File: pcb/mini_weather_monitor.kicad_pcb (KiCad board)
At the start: 2 copper layers, 135 x 72 mm, 28 parts, among them J1 Conn_01x02, Q1 IRLML6402, U2 4.0inch_SPI_MSP4021, U2_BME280 module_bme280, U3_BH1750 module_bh1750

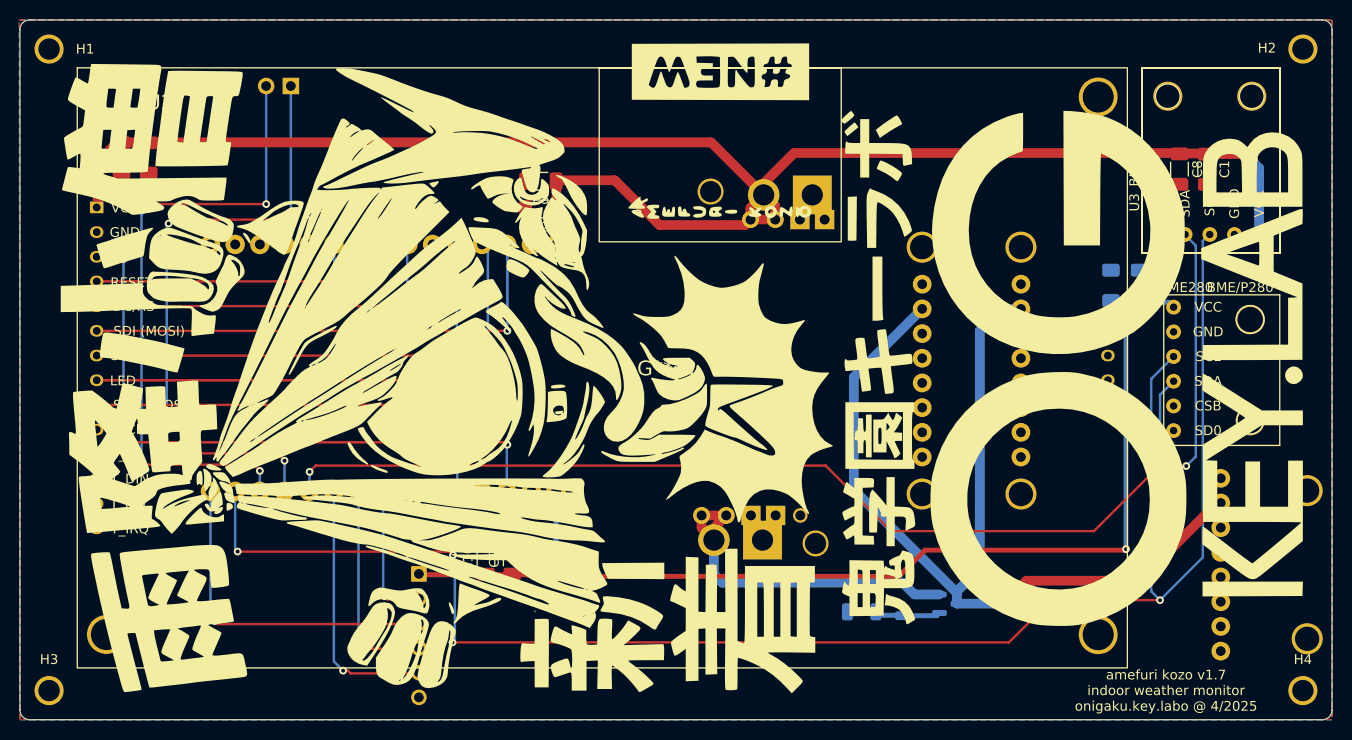
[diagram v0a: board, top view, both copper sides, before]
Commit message: adding passthrough
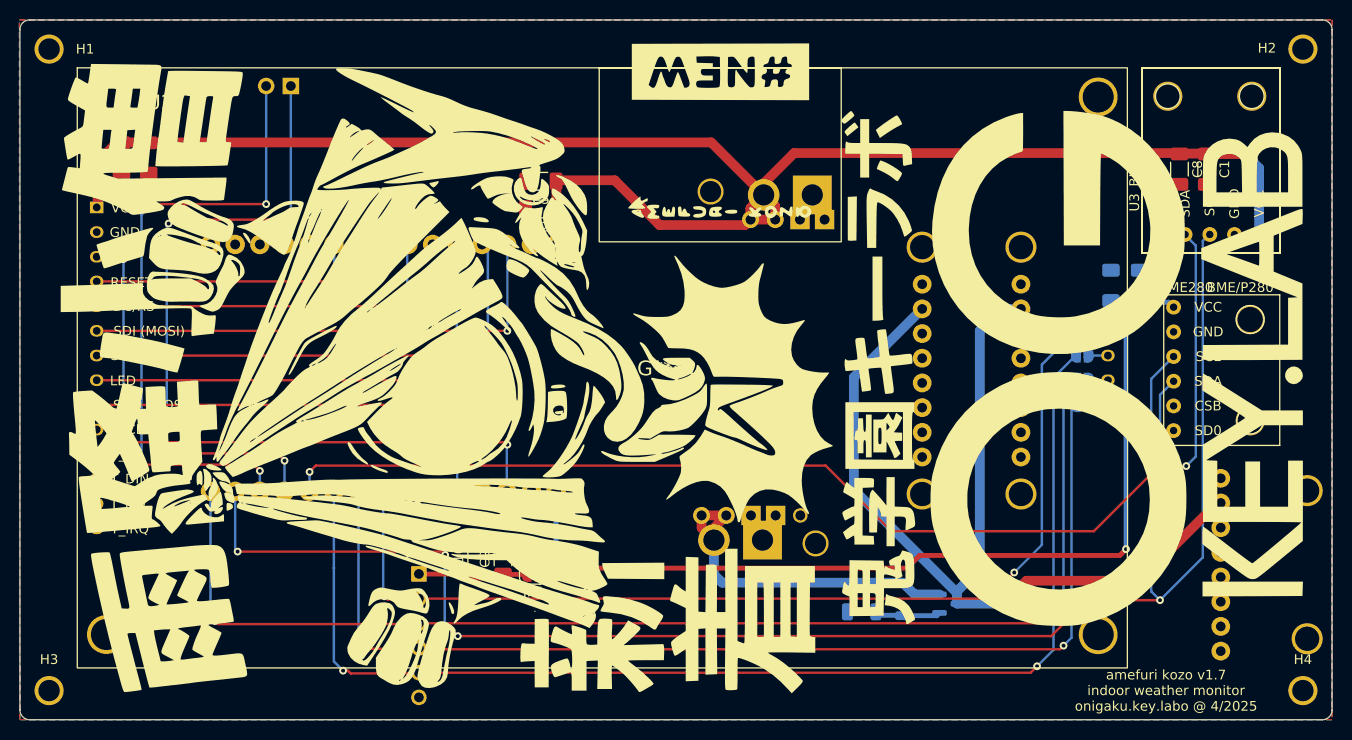
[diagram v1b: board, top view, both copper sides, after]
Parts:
- added JP5: sj_mini_3v3, Jumper:SolderJumper-2_P1.3mm_Open_RoundedPad1.0x1.5mm, F.Cu at (118.8, 121.0)
- added JP6: sj_Open_onboard_sdcard_MOSI, Jumper:SolderJumper-2_P1.3mm_Open_RoundedPad1.0x1.5mm, B.Cu at (175.3, 98.5)
- added JP7: sj_Open_onboard_sdcard_MISO, Jumper:SolderJumper-2_P1.3mm_Open_RoundedPad1.0x1.5mm, B.Cu at (175.3, 101.0)
- added JP8: sj_Open_onboard_sdcard_CS, Jumper:SolderJumper-2_P1.3mm_Open_RoundedPad1.0x1.5mm, B.Cu at (175.3, 96.0)
- added JP9: sj_onboard_sdcard_clk, Jumper:SolderJumper-2_P1.3mm_Open_RoundedPad1.0x1.5mm, B.Cu at (175.3, 103.6)
- moved C10 0.95 mm to (113.0, 119.5)
- moved C9 0.95 mm to (115.7, 119.5)
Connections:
- C10 pad 1: +3V3 -> Net-(JP5-B)
- C9 pad 1: +3V3 -> Net-(JP5-B)
- U2 pad 15: unconnected-(U2-SD_CS-Pad15) -> Net-(JP8-A)
- U2 pad 16: unconnected-(U2-SD_MOSI-Pad16) -> Net-(JP6-A)
- U2 pad 17: unconnected-(U2-SD_MISO-Pad17) -> Net-(JP7-A)
- U2 pad 18: unconnected-(U2-SD_SCK-Pad18) -> Net-(JP9-A)
- U3_minisdcard1 pad 1: +3V3 -> Net-(JP5-B)
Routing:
- net Net-(JP6-B): track 26.8 -> 124.5 mm, vias 1 -> 2
- net Net-(JP9-B): track 22.0 -> 113.9 mm, vias 1 -> 2
- net Net-(JP7-B): track 34.7 -> 125.6 mm, vias 1 -> 2
- net Net-(JP8-B): track 14.6 -> 104.5 mm, vias 1 -> 2
- net +3V3: track 115.2 -> 102.1 mm
- net Net-(JP5-B): track 0.00 -> 11.1 mm
- net Net-(JP6-A): track 0.00 -> 2.42 mm
- net Net-(JP8-A): track 0.00 -> 2.01 mm
- net Net-(JP7-A): track 0.00 -> 2.00 mm
- net Net-(JP9-A): track 0.00 -> 1.99 mm
- net Net-(U2_BME280-SCL): track 178.5 -> 176.6 mm

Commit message: slight retrace
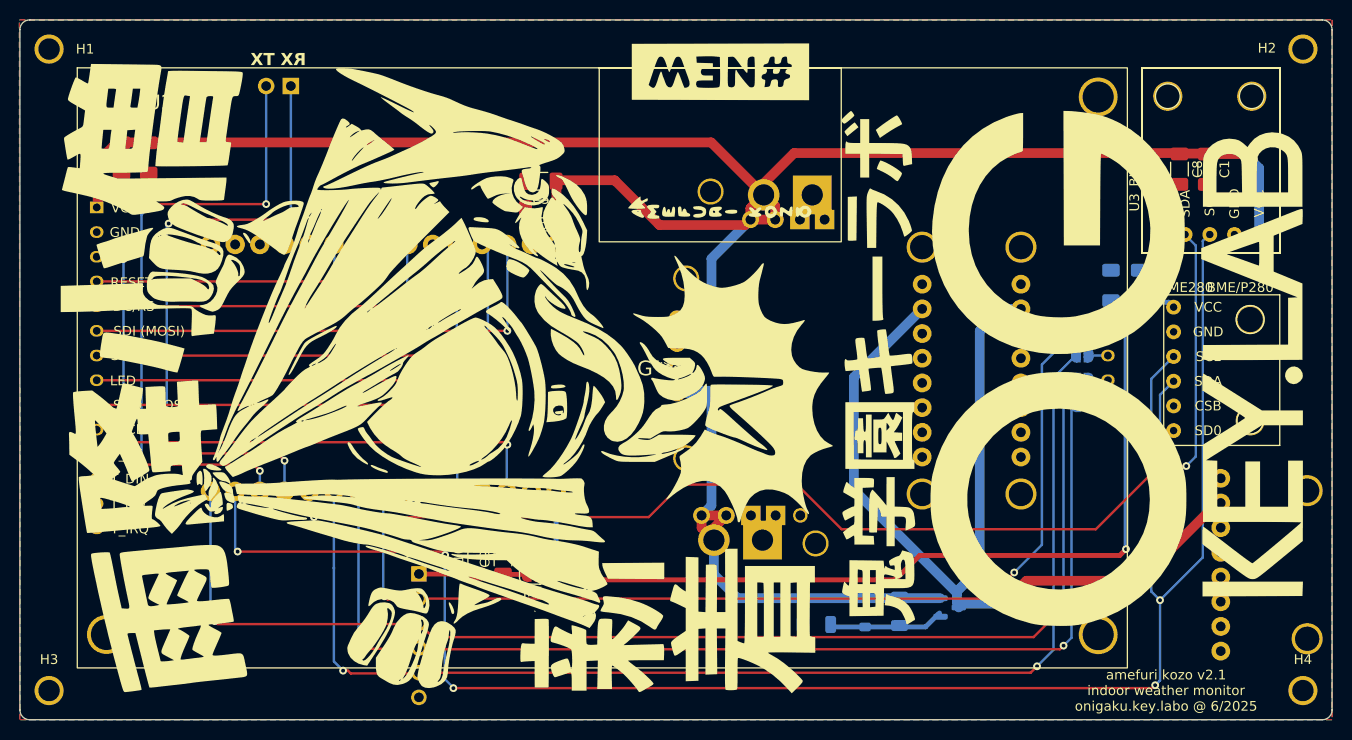
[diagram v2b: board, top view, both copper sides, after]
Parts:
- added JP1: s13v30f5_VIN, Jumper:SolderJumper-2_P1.3mm_Open_RoundedPad1.0x1.5mm, B.Cu at (136.5, 102.4)
- added JP2: s13v30f5_VOUT, Jumper:SolderJumper-2_P1.3mm_Open_RoundedPad1.0x1.5mm, B.Cu at (136.5, 94.8)
- added R2: 1k, Resistor_SMD:R_1206_3216Metric, B.Cu at (156.5, 124.8)
- added U3: S13v30F5, boost_converter:pololu S13V30F5 step up step down, B.Cu at (144.6, 99.8)
- U1: value ~ -> U3V70F5
- moved R1 4.83 mm to (147.9, 126.2)
- moved D1 3.87 mm to (152.9, 124.8)
- moved Q1 0.40 mm to (161.7, 124.5)
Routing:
- net VBUS: track 36.3 -> 49.5 mm
- net Net-(U2_BME280-SCL): track 176.6 -> 189.5 mm, vias 4 -> 5
- net VCC: track 179.5 -> 191.4 mm
- net Net-(D1-A): track 7.10 -> 12.7 mm
- net Net-(JP1-A): track 0.00 -> 2.24 mm
- net Net-(JP2-A): track 0.00 -> 2.23 mm
- net Net-(JP7-B): track 125.6 -> 126.8 mm
- net +3V3: track 102.1 -> 103.1 mm
- net Net-(U2_BME280-SDA): track 132.1 -> 132.6 mm
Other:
- board text added: "amefuri kozo v2.1 indoor weather monitor onigaku.key.labo @ 6/2025"
- board text removed: "amefuri kozo v1.7 indoor weather monitor onigaku.key.labo @ 4/2025"

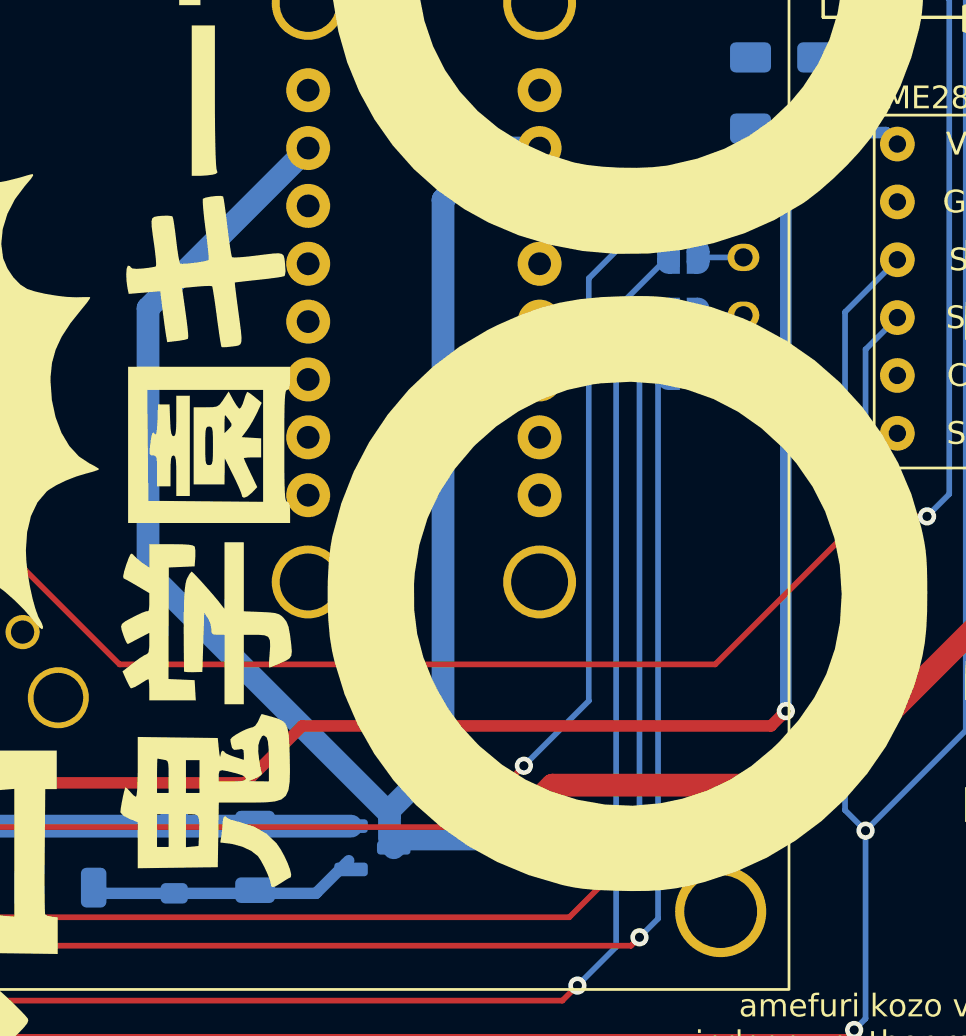
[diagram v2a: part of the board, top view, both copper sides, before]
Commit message: fixing forecast parsing and display
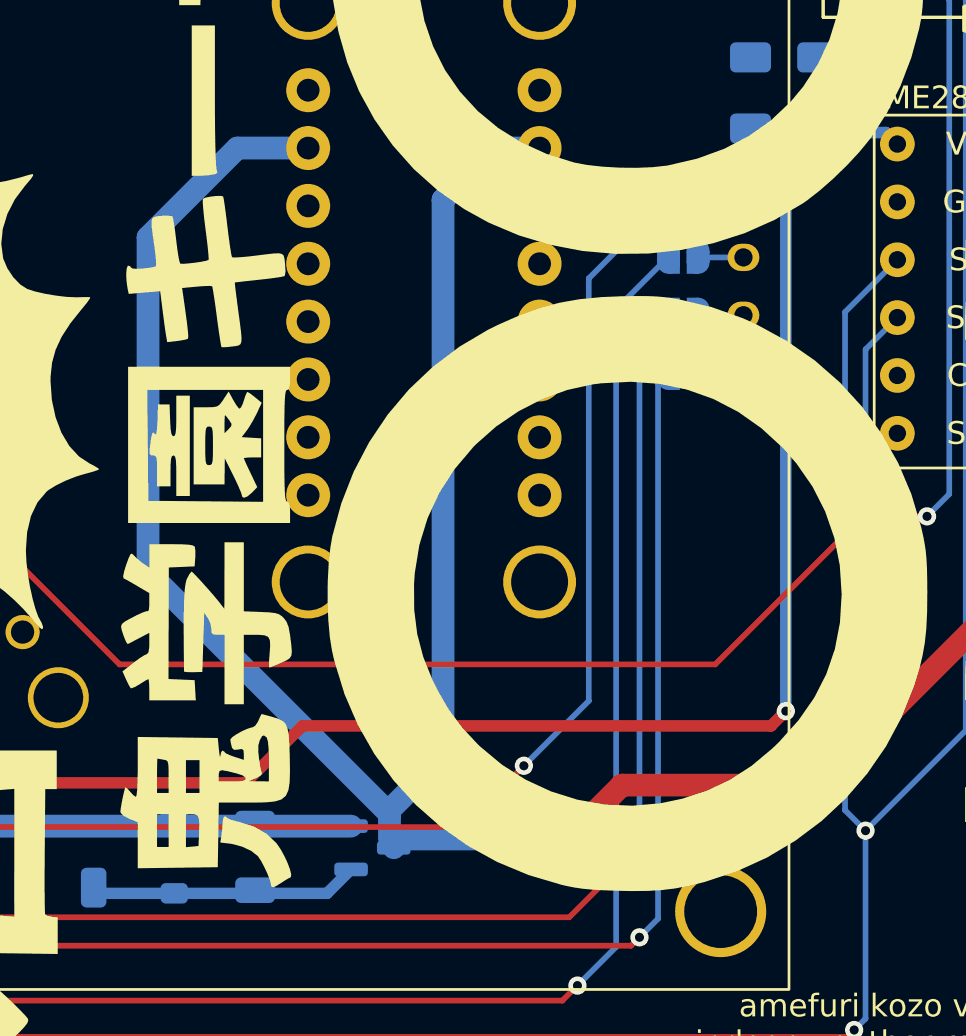
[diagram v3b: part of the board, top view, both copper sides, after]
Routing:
- net Net-(Q1-D): track 103.2 -> 105.0 mm
- net Net-(D1-A): track 12.7 -> 11.9 mm
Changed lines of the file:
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@@
 	)
 	(segment
-		(start 189.56 113.33)
-		(end 181.19 121.7)
+		(start 170.35 123.95)
+		(end 167.3 123.95)
 		(width 1)
 		(layer "F.Cu")
@@
 	)
 	(segment
-		(start 169.55 121.7)
-		(end 167.3 123.95)
+		(start 189.56 113.33)
+		(end 181.19 121.7)
+		(width 1)
+		(layer "F.Cu")
+		(net 55)
+	)
+	(segment
+		(start 172.6 121.7)
+		(end 170.35 123.95)
 		(width 1)
 		(layer "F.Cu")
@@
 	(segment
 		(start 181.19 121.7)
-		(end 169.55 121.7)
+		(end 172.6 121.7)
 		(width 1)
 		(layer "F.Cu")
@@
 		(drill 0.8)
 		(layers "F.Cu" "B.Cu")
+		(net 55)
+	)
+	(segment
+		(start 162.4 122.956262)
+		(end 151.8 112.356262)
+		(width 1)
+		(layer "B.Cu")
 		(net 55)
 	)
@@
 	)
 	(segment
-		(start 162.4 123)
-		(end 162.4 122.956262)
+		(start 151.8 112.356262)
+		(end 151.8 97.65)
 		(width 1)
 		(layer "B.Cu")
@@
 	)
 	(segment
-		(start 151.8 100.76)
+		(start 155.72 93.73)
 		(end 158.83 93.73)
 		(width 1)
@@
 	)
 	(segment
-		(start 162.4 122.956262)
-		(end 151.8 112.356262)
+		(start 151.8 97.65)
+		(end 155.72 93.73)
 		(width 1)
 		(layer "B.Cu")
@@
 		(end 167.3 123.95)
 		(width 0.25)
-		(layer "B.Cu")
-		(net 55)
-	)
-	(segment
-		(start 151.8 112.356262)
-		(end 151.8 100.76)
-		(width 1)
 		(layer "B.Cu")
 		(net 55)
@@
 	)
 	(segment
-		(start 160.7125 125.112498)
-		(end 160.612501 125.012499)
-		(width 0.25)
+		(start 162.4 123)
+		(end 162.4 122.956262)
+		(width 1)
 		(layer "B.Cu")
-		(net 56)
+		(net 55)
 	)
 	(segment
-		(start 149.4125 126.2)
-		(end 149.6625 126.45)
+		(start 159.662502 126.45)
+		(end 160.7125 125.400002)
 		(width 0.5)
 		(layer "B.Cu")
@@
 	)
 	(segment
-		(start 160.7125 125.4)
-		(end 160.7125 125.112498)
-		(width 0.25)
-		(layer "B.Cu")
-		(net 56)
-	)
-	(segment
-		(start 160.7125 125.3875)
-		(end 160.475 125.15)
-		(width 0.508)
+		(start 149.4125 126.2)
+		(end 149.6625 126.45)
+		(width 0.5)
 		(layer "B.Cu")
 		(net 56)
@@
 	(segment
 		(start 152.95 126.45)
-		(end 159.175 126.45)
+		(end 159.662502 126.45)
 		(width 0.5)
 		(layer "B.Cu")
-		(net 56)
-	)
-	(segment
-		(start 159.175 126.45)
-		(end 160.612501 125.012499)
-		(width 0.5)
-		(layer "B.Cu")
